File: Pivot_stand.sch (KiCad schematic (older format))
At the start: 6 parts, among them J1 USB_B_Micro, J2 Conn_01x02_Male, U1 IFX27001TFV33

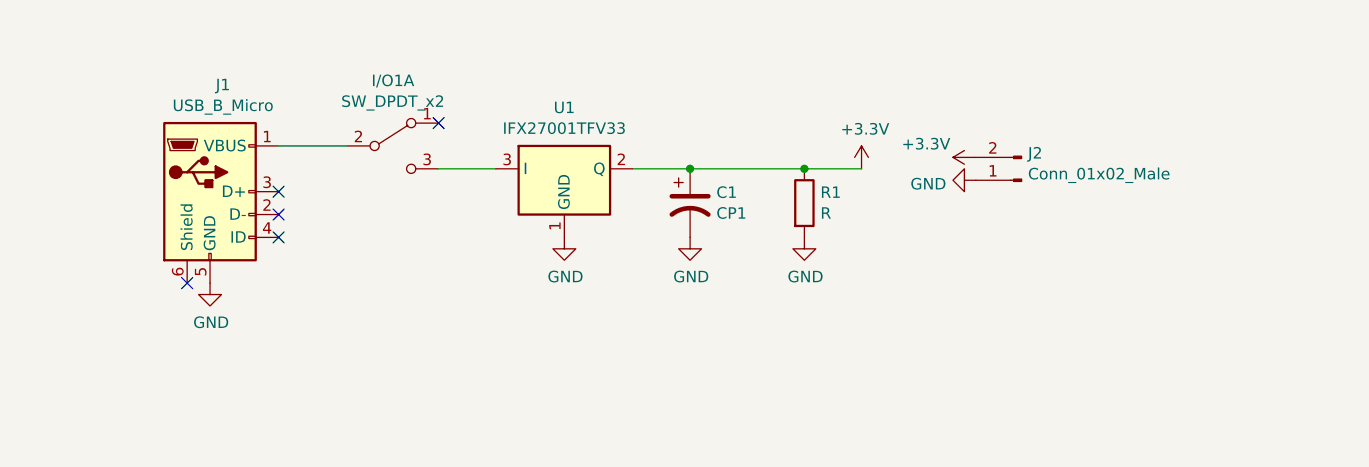
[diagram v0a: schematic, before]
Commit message: Improvements
Added resistor from pin 1 of regulator to ground to allow for Adj regulator to be used. Defaulted to 0 ohm.

Added 0 ohm resistor to voltage output. This allows a resistance to be added in to protect SAOs with no current limiting resistor on LEDs.

Tied USB shield to ground using 1M resistor and 0.1uF cap.
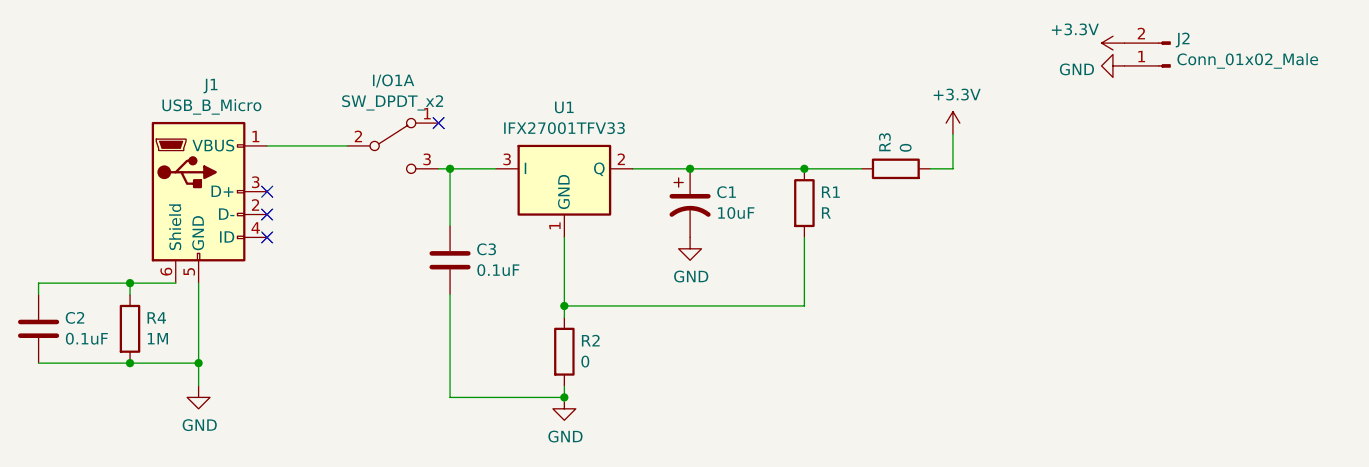
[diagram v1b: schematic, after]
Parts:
- added C2, C3: 0.1uF, Capacitor_SMD:C_0805_2012Metric_Pad1.18x1.45mm_HandSolder, symbol Device:C
- added R2, R3: 0, Resistor_SMD:R_1206_3216Metric, symbol Device:R
- added R4: 1M, Resistor_SMD:R_0603_1608Metric_Pad1.05x0.95mm_HandSolder, symbol Device:R
- C1: value CP1 -> 10uF
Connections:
- net +3V3: now also R3.2; no longer C1.1, R1.1, U1.2 (Q)
- net GND: now also C2.2, C3.2, R2.2, R4.2; no longer R1.2, U1.1 (GND)
- net at J1.6 (Shield): now also C2.1, R4.1
- net at I/O1.3 (C), U1.3 (I): now also C3.1
- new net: R1.2, R2.1, U1.1 (GND)
- new net: C1.1, R1.1, R3.1, U1.2 (Q)
- no-connect marks 5 -> 4
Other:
- moved on the sheet: J1, J2
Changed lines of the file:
@@
 L Connector:USB_B_Micro J1
 U 1 1 60E39C54
-P 4500 2800
-F 0 "J1" H 4557 3267 50  0000 C CNN
-F 1 "USB_B_Micro" H 4557 3176 50  0000 C CNN
-F 2 "Connector_USB:USB_Micro-B_Wuerth_629105150521" H 4650 2750 50  0001 C CNN
-F 3 "~" H 4650 2750 50  0001 C CNN
-	1    4500 2800
+P 4450 2800
+F 0 "J1" H 4507 3267 50  0000 C CNN
+F 1 "USB_B_Micro" H 4507 3176 50  0000 C CNN
+F 2 "Connector_USB:USB_Micro-B_Wuerth_629105150521" H 4600 2750 50  0001 C CNN
+F 3 "~" H 4600 2750 50  0001 C CNN
+	1    4450 2800
 	1    0    0    -1
 $EndComp
@@
 L power:GND #PWR0101
 U 1 1 60E3B963
-P 4500 3200
-F 0 "#PWR0101" H 4500 2950 50  0001 C CNN
-F 1 "GND" H 4505 3027 50  0000 C CNN
-F 2 "" H 4500 3200 50  0001 C CNN
-F 3 "" H 4500 3200 50  0001 C CNN
-	1    4500 3200
+P 4450 3650
+F 0 "#PWR0101" H 4450 3400 50  0001 C CNN
+F 1 "GND" H 4455 3477 50  0000 C CNN
+F 2 "" H 4450 3650 50  0001 C CNN
+F 3 "" H 4450 3650 50  0001 C CNN
+	1    4450 3650
 	1    0    0    -1
 $EndComp
@@
 L power:GND #PWR0103
 U 1 1 60E3F785
-P 6050 3000
-F 0 "#PWR0103" H 6050 2750 50  0001 C CNN
-F 1 "GND" H 6055 2827 50  0000 C CNN
-F 2 "" H 6050 3000 50  0001 C CNN
-F 3 "" H 6050 3000 50  0001 C CNN
-	1    6050 3000
+P 6050 3700
+F 0 "#PWR0103" H 6050 3450 50  0001 C CNN
+F 1 "GND" H 6055 3527 50  0000 C CNN
+F 2 "" H 6050 3700 50  0001 C CNN
+F 3 "" H 6050 3700 50  0001 C CNN
+	1    6050 3700
 	1    0    0    -1
 $EndComp
@@
 P 6600 2850
 F 0 "C1" H 6715 2896 50  0000 L CNN
-F 1 "CP1" H 6715 2805 50  0000 L CNN
+F 1 "10uF" H 6715 2805 50  0000 L CNN
 F 2 "Capacitor_SMD:C_0805_2012Metric" H 6600 2850 50  0001 C CNN
 F 3 "~" H 6600 2850 50  0001 C CNN
@@
 	1    0    0    -1
 $EndComp
-$Comp
-L power:GND #PWR0105
-U 1 1 60E42B2E
-P 7100 3000
-F 0 "#PWR0105" H 7100 2750 50  0001 C CNN
-F 1 "GND" H 7105 2827 50  0000 C CNN
-F 2 "" H 7100 3000 50  0001 C CNN
-F 3 "" H 7100 3000 50  0001 C CNN
-	1    7100 3000
-	1    0    0    -1
-$EndComp
 Wire Wire Line
 	6350 2700 6600 2700
@@
 	6600 2700 7100 2700
 Connection ~ 7100 2700
-NoConn ~ 4800 2800
-NoConn ~ 4800 3000
-NoConn ~ 4800 2900
-NoConn ~ 4400 3200
+NoConn ~ 4750 2800
+NoConn ~ 4750 3000
+NoConn ~ 4750 2900
 Wire Wire Line
 	7100 2700 7350 2700
@@
 L power:GND #PWR0102
 U 1 1 60E489CF
-P 7850 2750
-F 0 "#PWR0102" H 7850 2500 50  0001 C CNN
-F 1 "GND" V 7867 2621 50  0000 R CNN
-F 2 "" H 7850 2750 50  0001 C CNN
-F 3 "" H 7850 2750 50  0001 C CNN
-	1    7850 2750
+P 8500 2250
+F 0 "#PWR0102" H 8500 2000 50  0001 C CNN
+F 1 "GND" V 8517 2121 50  0000 R CNN
+F 2 "" H 8500 2250 50  0001 C CNN
+F 3 "" H 8500 2250 50  0001 C CNN
+	1    8500 2250
 	0    1    1    0
 $EndComp
@@
 L power:+3.3V #PWR0106
 U 1 1 60E492DA
-P 7350 2700
-F 0 "#PWR0106" H 7350 2550 50  0001 C CNN
-F 1 "+3.3V" H 7365 2873 50  0000 C CNN
-F 2 "" H 7350 2700 50  0001 C CNN
-F 3 "" H 7350 2700 50  0001 C CNN
-	1    7350 2700
+P 7750 2550
+F 0 "#PWR0106" H 7750 2400 50  0001 C CNN
+F 1 "+3.3V" H 7765 2723 50  0000 C CNN
+F 2 "" H 7750 2550 50  0001 C CNN
+F 3 "" H 7750 2550 50  0001 C CNN
+	1    7750 2550
 	1    0    0    -1
 $EndComp
@@
 L Connector:Conn_01x02_Male J2
 U 1 1 60E4666C
-P 8050 2750
-F 0 "J2" H 8022 2632 50  0000 R CNN
-F 1 "Conn_01x02_Male" H 8022 2723 50  0000 R CNN
-F 2 "Connector_PinHeader_2.00mm:PinHeader_1x02_P2.00mm_Vertical" H 8050 2750 50  0001 C CNN
-F 3 "~" H 8050 2750 50  0001 C CNN
-	1    8050 2750
+P 8700 2250
+F 0 "J2" H 8672 2132 50  0000 R CNN
+F 1 "Conn_01x02_Male" H 8672 2223 50  0000 R CNN
+F 2 "Connector_PinHeader_2.00mm:PinHeader_1x02_P2.00mm_Vertical" H 8700 2250 50  0001 C CNN
+F 3 "~" H 8700 2250 50  0001 C CNN
+	1    8700 2250
 	-1   0    0    1
 $EndComp
@@
 NoConn ~ 5500 2500
 Wire Wire Line
-	4800 2600 5100 2600
-Wire Wire Line
-	5750 2700 5500 2700
+	5750 2700 5550 2700
 $Comp
 L power:+3.3V #PWR0107
 U 1 1 60E49B1D
-P 7850 2650
-F 0 "#PWR0107" H 7850 2500 50  0001 C CNN
-F 1 "+3.3V" V 7908 2868 50  0000 C CNN
-F 2 "" H 7850 2650 50  0001 C CNN
-F 3 "" H 7850 2650 50  0001 C CNN
-	1    7850 2650
+P 8500 2150
+F 0 "#PWR0107" H 8500 2000 50  0001 C CNN
+F 1 "+3.3V" V 8558 2368 50  0000 C CNN
+F 2 "" H 8500 2150 50  0001 C CNN
+F 3 "" H 8500 2150 50  0001 C CNN
+	1    8500 2150
 	0    -1   -1   0
 $EndComp
+$Comp
+L Device:R R2
+U 1 1 634C8F07
+P 6050 3500
+F 0 "R2" H 6120 3546 50  0000 L CNN
+F 1 "0" H 6120 3455 50  0000 L CNN
+F 2 "Resistor_SMD:R_1206_3216Metric" V 5980 3500 50  0001 C CNN
+F 3 "~" H 6050 3500 50  0001 C CNN
+	1    6050 3500
+	1    0    0    -1
+$EndComp
+Wire Wire Line
+	4750 2600 5100 2600
+Wire Wire Line
+	6050 3000 6050 3300
+Wire Wire Line
+	7100 3000 7100 3300
+Wire Wire Line
+	7100 3300 6050 3300
+Connection ~ 6050 3300
+Wire Wire Line
+	6050 3300 6050 3350
+$Comp
+L Device:R R3
+U 1 1 634CE49D
+P 7500 2700
+F 0 "R3" H 7570 2746 50  0000 L CNN
+F 1 "0" H 7570 2655 50  0000 L CNN
+F 2 "Resistor_SMD:R_1206_3216Metric" V 7430 2700 50  0001 C CNN
+F 3 "~" H 7500 2700 50  0001 C CNN
+	1    7500 2700
+	0    -1   -1   0
+$EndComp
+Wire Wire Line
+	7650 2700 7750 2700
+Wire Wire Line
+	7750 2700 7750 2550
+Wire Wire Line
+	6050 3650 6050 3700
+$Comp
+L Device:R R4
+U 1 1 634CF86B
+P 4150 3400
+F 0 "R4" H 4220 3446 50  0000 L CNN
+F 1 "1M" H 4220 3355 50  0000 L CNN
+F 2 "Resistor_SMD:R_0603_1608Metric_Pad1.05x0.95mm_HandSolder" V 4080 3400 50  0001 C CNN
+F 3 "~" H 4150 3400 50  0001 C CNN
+	1    4150 3400
+	1    0    0    -1
+$EndComp
+$Comp
+L Device:C C2
+U 1 1 634CFDF9
+P 3750 3400
+F 0 "C2" H 3865 3446 50  0000 L CNN
+F 1 "0.1uF" H 3865 3355 50  0000 L CNN
+F 2 "Capacitor_SMD:C_0805_2012Metric_Pad1.18x1.45mm_HandSolder" H 3788 3250 50  0001 C CNN
+F 3 "~" H 3750 3400 50  0001 C CNN
+	1    3750 3400
+	1    0    0    -1
+$EndComp
+Wire Wire Line
+	4350 3200 4150 3200
+Wire Wire Line
+	4150 3200 4150 3250
+Wire Wire Line
+	3750 3250 3750 3200
+Wire Wire Line
+	3750 3200 4150 3200
+Connection ~ 4150 3200
+Wire Wire Line
+	4150 3550 4450 3550
+Wire Wire Line
+	4450 3200 4450 3550
+Connection ~ 4450 3550
+Wire Wire Line
+	4450 3550 4450 3650
+Wire Wire Line
+	3750 3550 4150 3550
+Connection ~ 4150 3550
+$Comp
+L Device:C C3
+U 1 1 634D2767
+P 5550 3100
+F 0 "C3" H 5665 3146 50  0000 L CNN
+F 1 "0.1uF" H 5665 3055 50  0000 L CNN
+F 2 "Capacitor_SMD:C_0805_2012Metric_Pad1.18x1.45mm_HandSolder" H 5588 2950 50  0001 C CNN
+F 3 "~" H 5550 3100 50  0001 C CNN
+	1    5550 3100
+	1    0    0    -1
+$EndComp
+Wire Wire Line
+	5550 2950 5550 2700
+Connection ~ 5550 2700
+Wire Wire Line
+	5550 2700 5500 2700
+Wire Wire Line
+	5550 3250 5550 3700
+Wire Wire Line
+	5550 3700 6050 3700
+Connection ~ 6050 3700
 $EndSCHEMATC
